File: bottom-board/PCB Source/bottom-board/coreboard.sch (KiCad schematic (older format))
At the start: 33 parts, among them J1 AS0A823-H4SB-7H, P5 HMI_DATA, P8 SERIAL_DEBUG, U4 AT24CS08-STUM

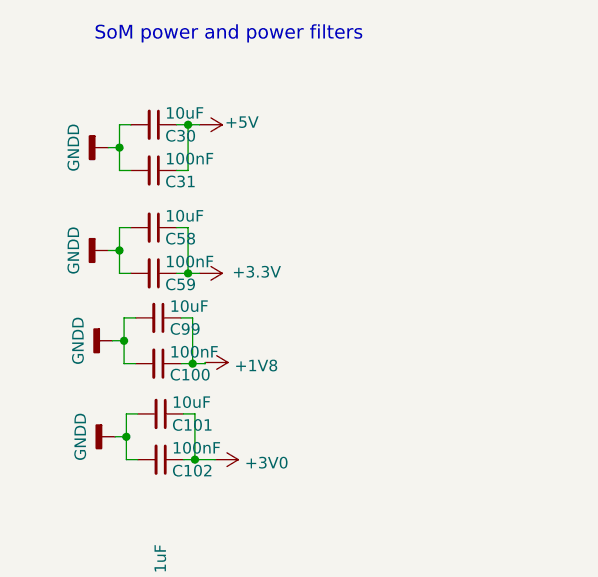
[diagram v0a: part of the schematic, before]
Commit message: increase som filter caps
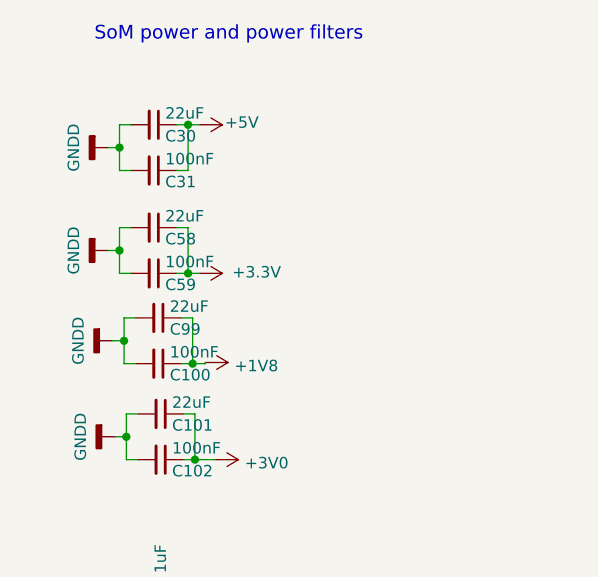
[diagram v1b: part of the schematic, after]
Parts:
- C101, C30, C58, C99: value 10uF -> 22uF; MPN GRM219R61E106KA12D -> CL21A226MPQNNNE
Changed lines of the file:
@@
 P 1320 1165
 F 0 "C30" V 1370 1215 50  0000 L CNN
-F 1 "10uF" V 1270 1215 50  0000 L CNN
+F 1 "22uF" V 1270 1215 50  0000 L CNN
 F 2 "Capacitor_SMD:C_0805_2012Metric" H 1320 1165 60  0001 C CNN
 F 3 "" H 1320 1165 60  0000 C CNN
-F 4 "GRM219R61E106KA12D" H -3980 -4185 50  0001 C CNN "MPN"
+F 4 "CL21A226MPQNNNE" H -3980 -4185 50  0001 C CNN "MPN"
 	1    1320 1165
 	0    1    1    0
@@
 P 1320 1615
 F 0 "C58" V 1370 1665 50  0000 L CNN
-F 1 "10uF" V 1270 1665 50  0000 L CNN
+F 1 "22uF" V 1270 1665 50  0000 L CNN
 F 2 "Capacitor_SMD:C_0805_2012Metric" H 1320 1615 60  0001 C CNN
 F 3 "" H 1320 1615 60  0000 C CNN
-F 4 "GRM219R61E106KA12D" H -3980 -3735 50  0001 C CNN "MPN"
+F 4 "CL21A226MPQNNNE" H -3980 -3735 50  0001 C CNN "MPN"
 	1    1320 1615
 	0    1    1    0
@@
 P 1340 2010
 F 0 "C99" V 1390 2060 50  0000 L CNN
-F 1 "10uF" V 1290 2060 50  0000 L CNN
+F 1 "22uF" V 1290 2060 50  0000 L CNN
 F 2 "Capacitor_SMD:C_0805_2012Metric" H 1340 2010 60  0001 C CNN
 F 3 "" H 1340 2010 60  0000 C CNN
-F 4 "GRM219R61E106KA12D" H -3960 -3340 50  0001 C CNN "MPN"
+F 4 "CL21A226MPQNNNE" H -3960 -3340 50  0001 C CNN "MPN"
 	1    1340 2010
 	0    1    1    0
@@
 P 1350 2430
 F 0 "C101" V 1400 2480 50  0000 L CNN
-F 1 "10uF" V 1300 2480 50  0000 L CNN
+F 1 "22uF" V 1300 2480 50  0000 L CNN
 F 2 "Capacitor_SMD:C_0805_2012Metric" H 1350 2430 60  0001 C CNN
 F 3 "" H 1350 2430 60  0000 C CNN
-F 4 "GRM219R61E106KA12D" H -3950 -2920 50  0001 C CNN "MPN"
+F 4 "CL21A226MPQNNNE" H -3950 -2920 50  0001 C CNN "MPN"
 	1    1350 2430
 	0    1    1    0
